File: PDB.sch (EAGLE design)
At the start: 31 parts, among them J1_CONNECTOR_INPUT 5566-4, U1 MICROCHIP_MIC29300-3_3WUMICRO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, U2 MIC29300-5.0WU-TR

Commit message: wiring complete
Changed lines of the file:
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@@
 <pinref part="C3" gate="G$1" pin="2"/>
 <wire x1="91.44" y1="88.9" x2="91.44" y2="86.36" width="0.1524" layer="91"/>
-<label x="88.9" y="83.82" size="1.778" layer="95"/>
+<label x="91.44" y="83.82" size="1.778" layer="95"/>
 </segment>
 <segment>
@@
 </sheet>
 </sheets>
+<errors>
+</errors>
 </schematic>
 </drawing>

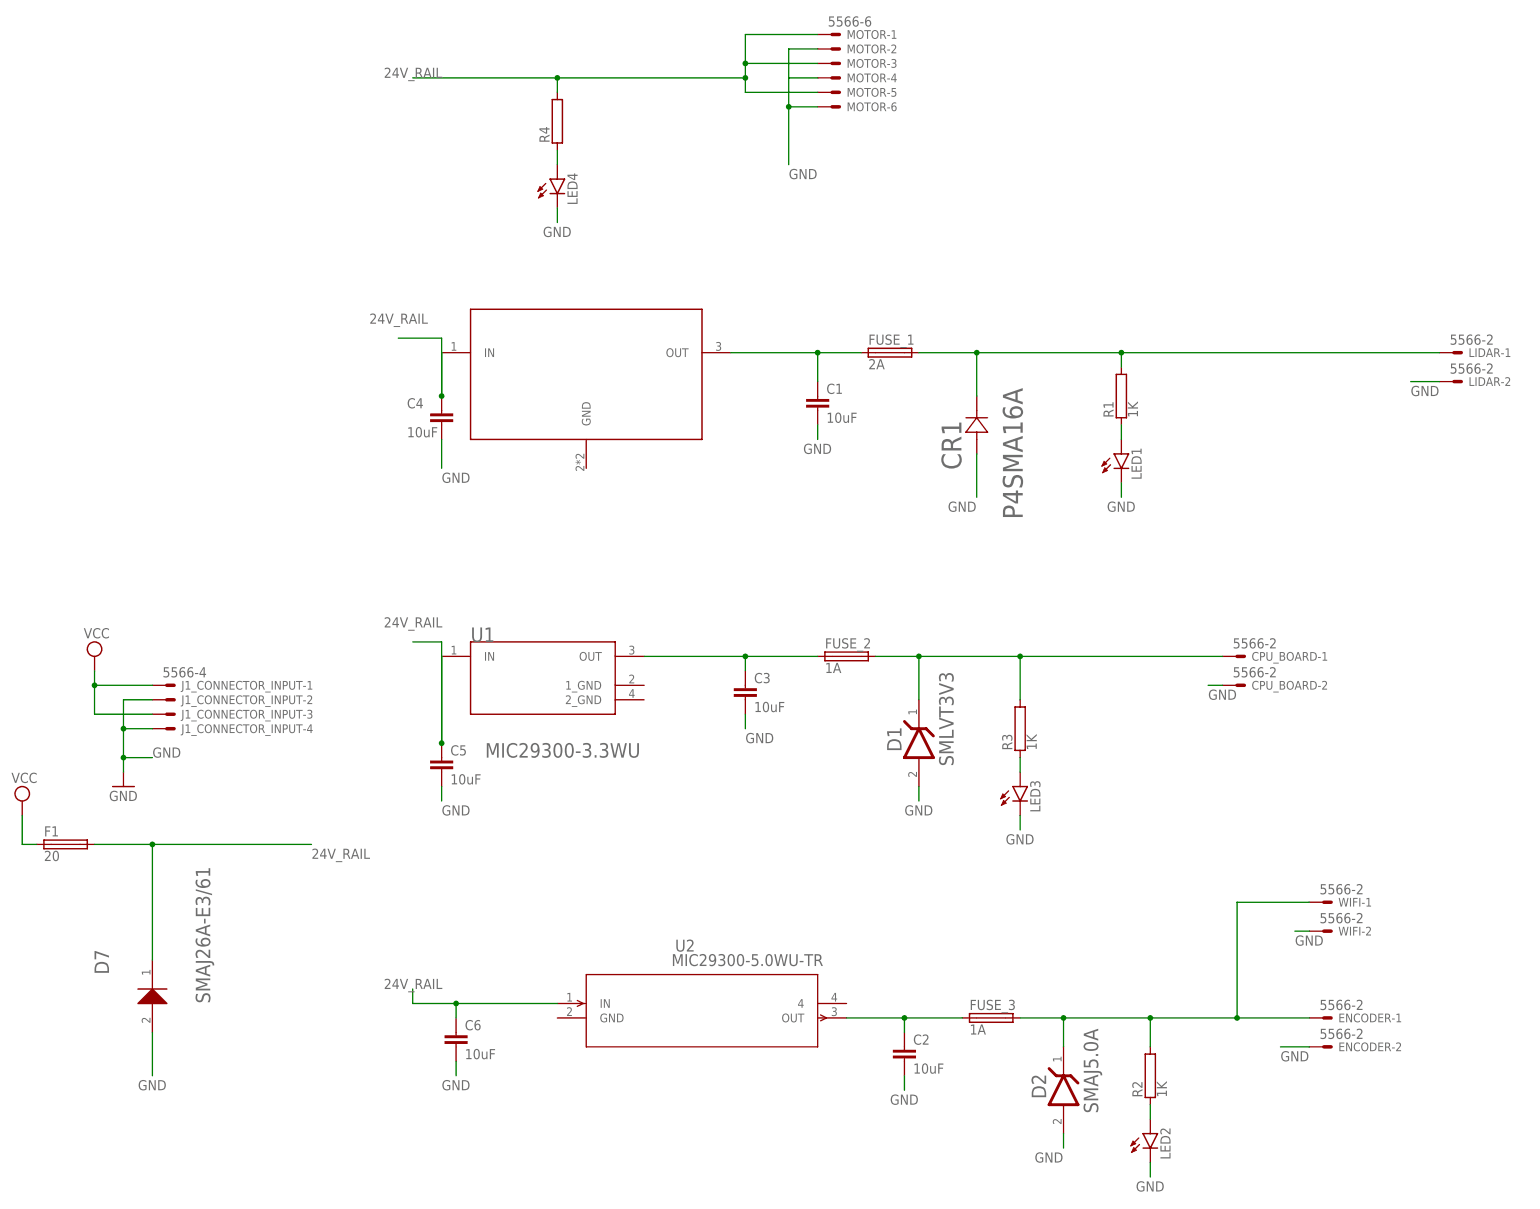
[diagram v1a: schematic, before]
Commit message: Updated MIC2930 linear regulators to all use the same symbol and footprint. Fixed all warnings and errors with schematic and board.
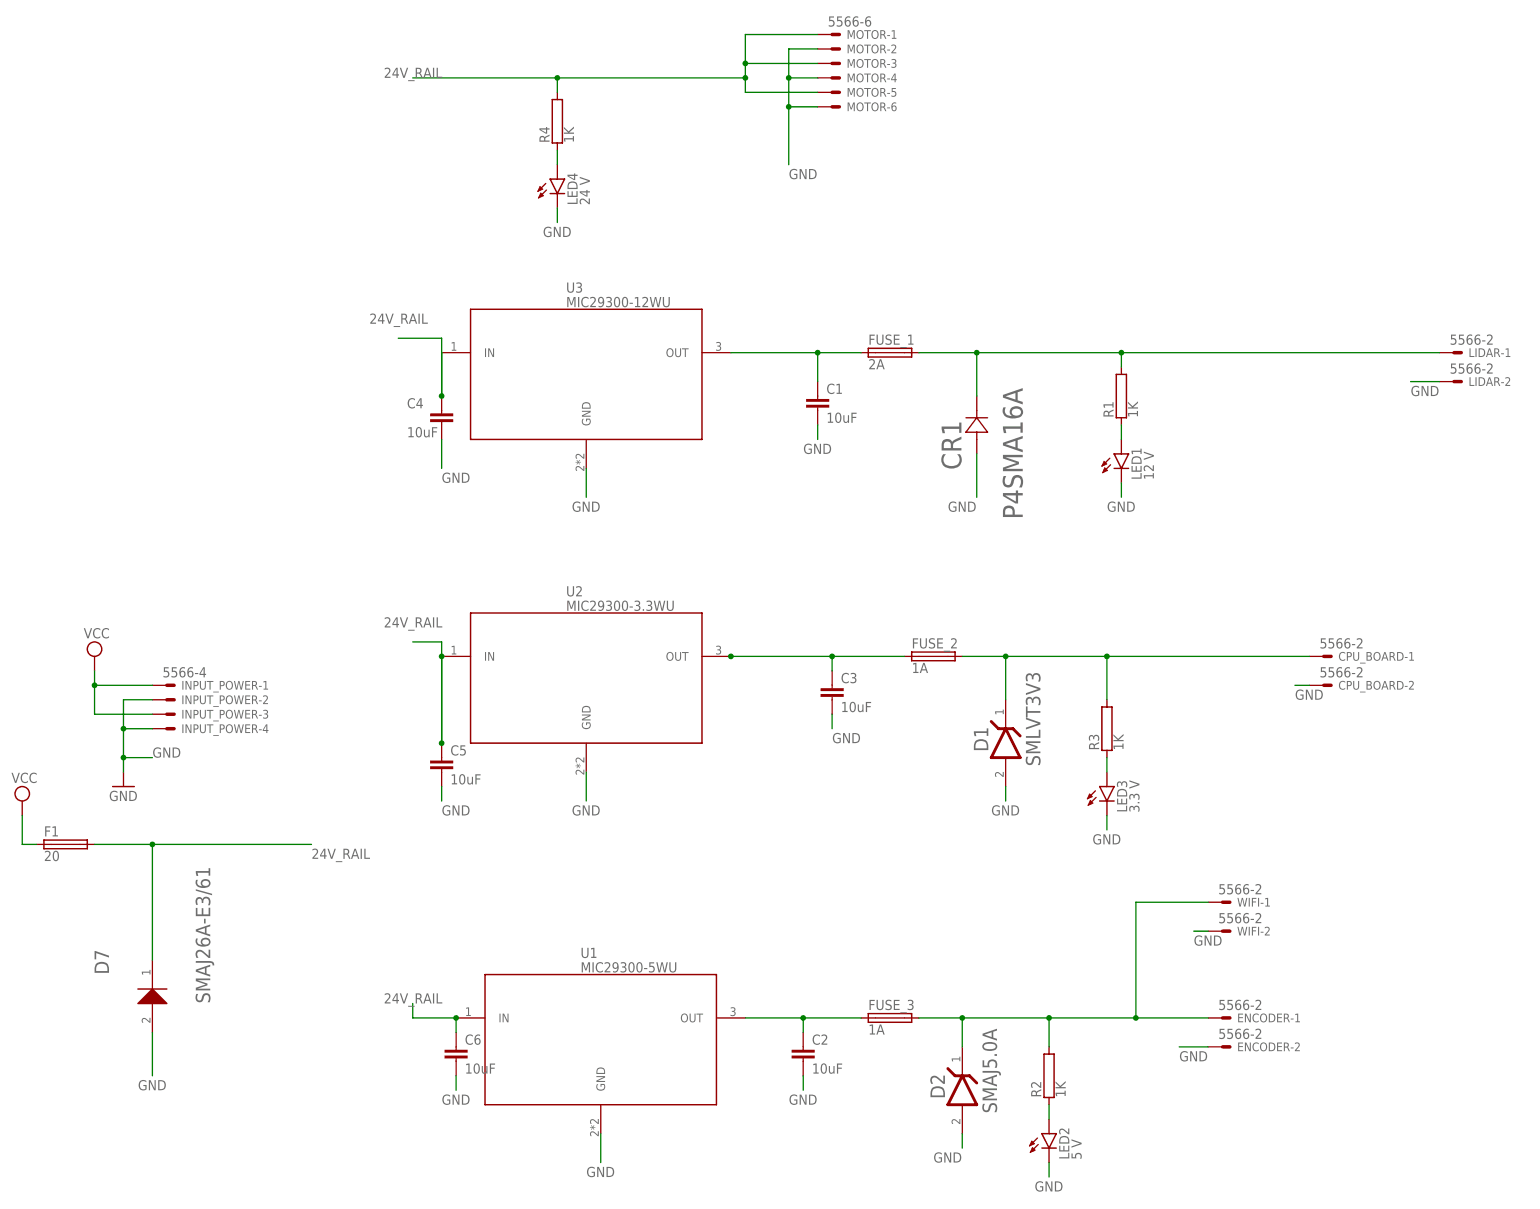
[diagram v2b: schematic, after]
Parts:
- removed U$1: MIC29300-12WU, MIC29300-12WU:MIC29300-12WU
- added U3: MIC29300-12WU, MIC29300:MIC29300-12WU
- LED1: value (none) -> 12 V
- LED2: value (none) -> 5 V
- LED3: value (none) -> 3.3 V
- LED4: value (none) -> 24 V
- R4: value (none) -> 1K
- U1: value MICROCHIP_MIC29300-3_3WUMICROCHIP_MIC29300-3_3WU_0_0 -> MIC29300-5WU; device Microchip - MIC29300-3.3WU:MICROCHIP_MIC29300-3_3WUMICROCHIP_MIC29300-3_3WU_0_0 -> MIC29300:MIC29300-5WU
- U2: value MIC29300-5.0WU-TR -> MIC29300-3.3WU; device mic29300-5v:MIC29300-5.0WU-TR -> MIC29300:MIC29300-3.3WU
- renumbered J1_CONNECTOR_INPUT to INPUT_POWER
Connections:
- net 24V_RAIL: now also U3.IN; no longer U$1.IN
- net GND: now also U1.GND, U2.GND, U3.GND
- net N$1: now also U3.OUT; no longer U$1.OUT
- net N$3: now also U1.OUT; no longer U2.OUT
- net N$4: now also U2.OUT; no longer U1.OUT
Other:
- moved on the sheet: C2, C3, C6, CPU_BOARD-1, CPU_BOARD-2, D1, D2, ENCODER-1, ENCODER-2, FUSE_2, FUSE_3, LED2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
